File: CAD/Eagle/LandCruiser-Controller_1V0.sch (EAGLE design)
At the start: 21 parts, among them U101 MEGA8-P, X301 I2C

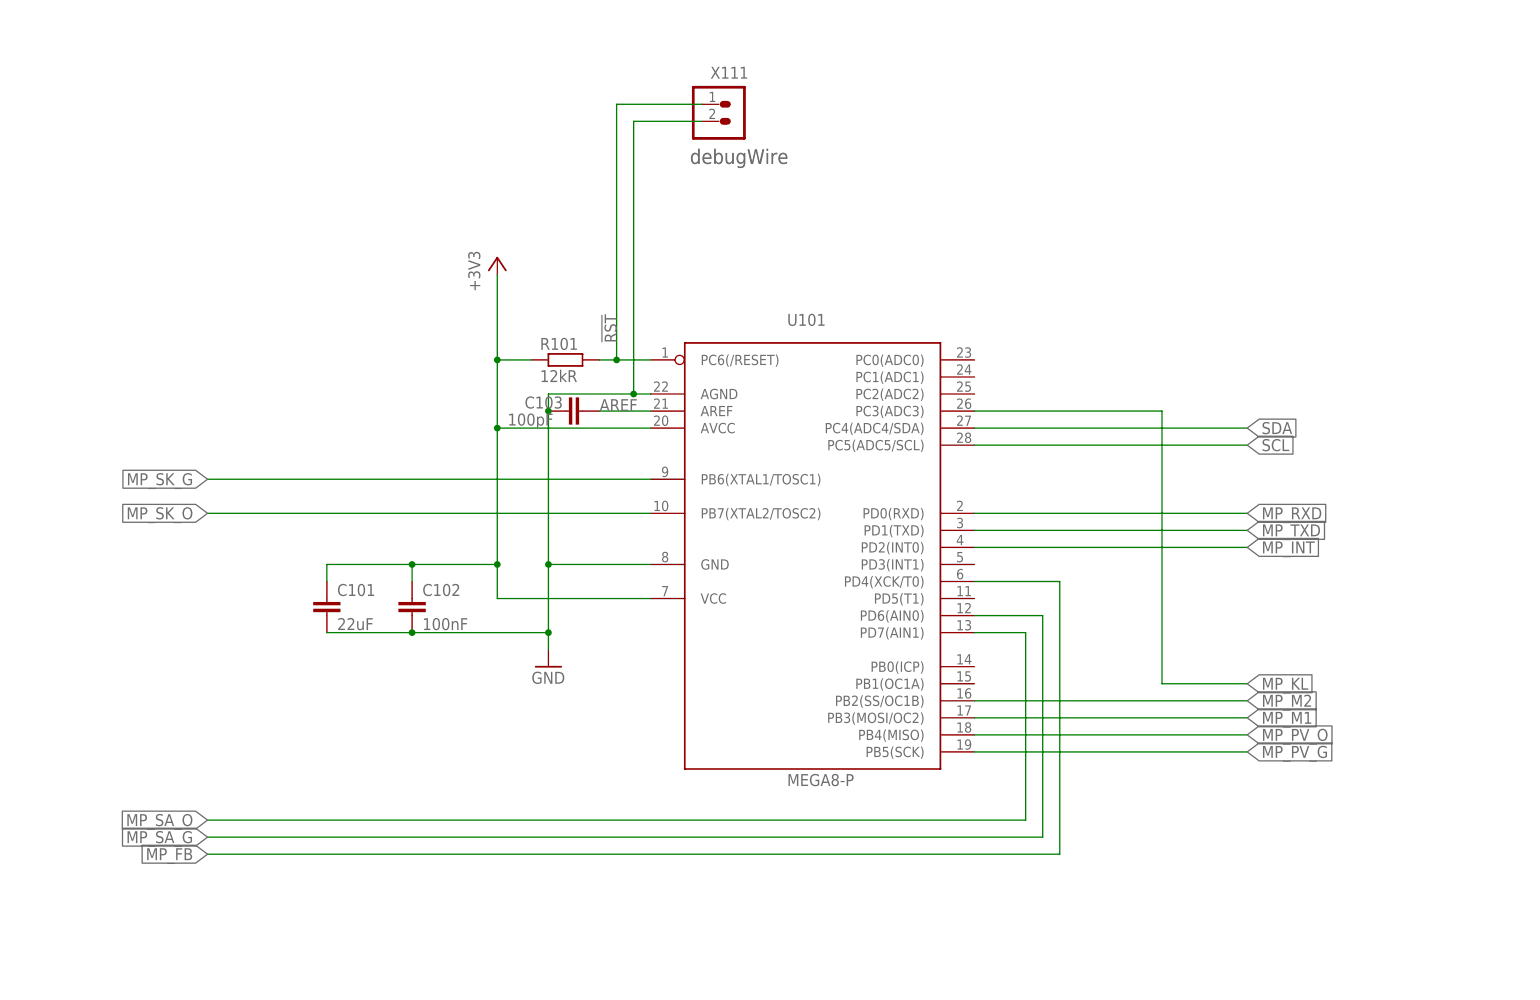
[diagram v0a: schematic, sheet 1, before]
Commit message: HW - pull-down resistors added to the ATmega output lines
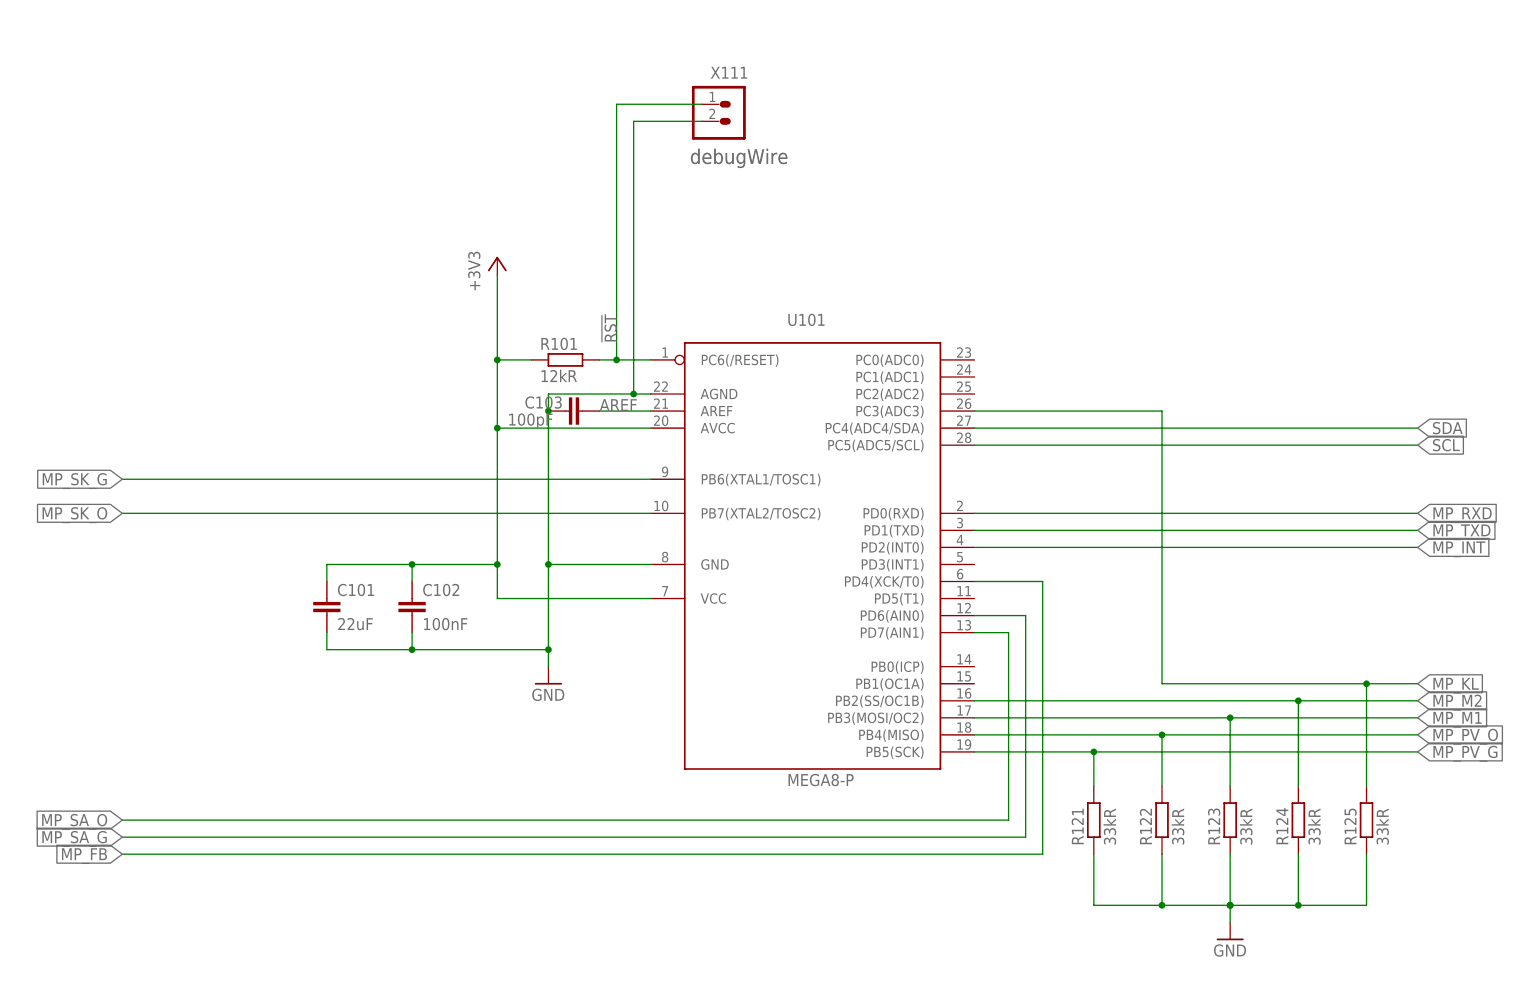
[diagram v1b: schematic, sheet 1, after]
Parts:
- added R121, R122, R123, R124, R125: 33kR, rcl:R-EU_0309/12
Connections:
- net GND: now also R121.1, R122.1, R123.1, R124.1, R125.1
- net MP_KL: now also R125.2
- net MP_M1: now also R123.2
- net MP_M2: now also R124.2
- net MP_PV_G: now also R121.2
- net MP_PV_O: now also R122.2

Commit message: HW - pull-up resistors added to the ATmega input lines
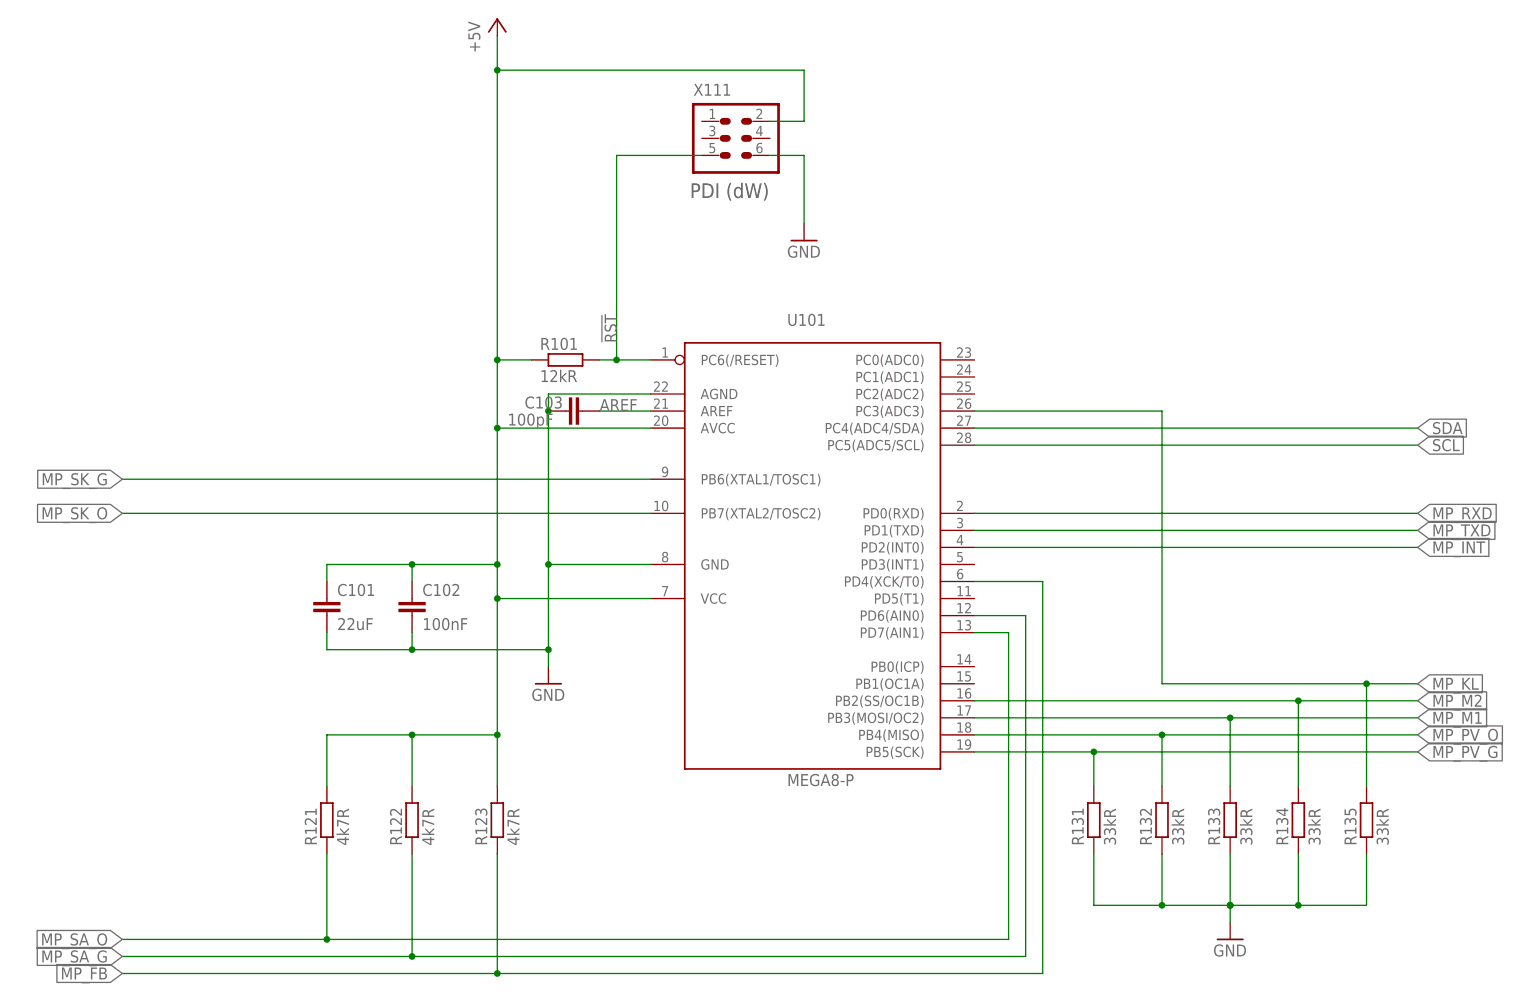
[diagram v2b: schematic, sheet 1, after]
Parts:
- removed C302: 100nF, rcl:C-EU050-035X075
- added R131, R132, R133: 33kR, rcl:R-EU_0309/12
- R121, R122, R123: value 33kR -> 4k7R
- R391, R392: value 1kR -> 2k2R
- X111: device df4iah_connector:HEADER-1X2 -> df4iah_connector:HEADER-2X3
- renumbered R124 to R134, R125 to R135
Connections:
- removed net +3V3: C101.1, C102.1, C302.1, R101.1, R391.2, R392.2, U101.AVCC, U101.VCC@1, X301.5
- net !RST: now also X111.5; no longer X111.1
- net +5V: now also C101.1, C102.1, R101.1, R121.2, R122.2, R123.2, R391.2, R392.2, U101.AVCC, U101.VCC@1, X111.2
- net GND: now also R131.1, R132.1, R133.1, X111.6; no longer C302.2, R121.1, R122.1, R123.1, X111.2
- net MP_FB: now also R123.1
- net MP_M1: now also R133.2; no longer R123.2
- net MP_PV_G: now also R131.2; no longer R121.2
- net MP_PV_O: now also R132.2; no longer R122.2
- net MP_SA_G: now also R122.1
- net MP_SA_O: now also R121.1
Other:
- note added: "PDI (dW)"
- note removed: "debugWire"
- moved on the sheet: R121, R122, R123, R391, R392

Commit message: HW - Linear voltage regulator 7805 added
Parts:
- removed C103: 100pF, rcl:C-EU050-035X075
- removed FM501, FM502, FM503, FM504: FIDUCIAL_MARK_1MM, df4iah_fiducial:FIDUCIAL_MARK_1MM
- added C501, C511: 22uF, rcl:CPOL-EUE2.5-7
- added U501: (no value), df4iah_powersupply:7805T
- C101: value 22uF -> 100nF; device rcl:C-EU150-084X183 -> rcl:C-EU050-035X075
- C102: value 100nF -> 100pF
- renumbered H501 to H603, H502 to H601, H503 to H604, H504 to H602, H511 to H611, H512 to H612
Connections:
- new net +12V: C501.+, U501.VI
- net +5V: now also C511.+, U501.VO; no longer C102.1
- net AREF: now also C102.2; no longer C103.2
- net GND: now also C102.1, C501.-, C511.-; no longer C102.2, C103.1
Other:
- note added: "X111-1 = N.C. X111-2 = VTG X111-3 = N.C. X111-4 = N.C. X111-5 = debugWIRE X111-6 = GND"

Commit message: HW - Wire-to-Board connectors added
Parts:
- added F501: 500 mA (S), fuse:SH22,5
- added R211, R212, R213, R214, R215: 12kR, rcl:R-EU_0309/12
- added X201, X321: WEIDMUELLER 1234600000, df4iah_connector:WIRE-TO-BOARD_5MM08_1X08
- renumbered C511 to C521, U501 to U511
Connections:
- new net +UB: F501.1, X201.8
- new net N$1: R211.1, X201.1
- new net N$10: X321.5
- new net N$2: R212.1, X201.2
- new net N$3: R213.1, X201.3
- new net N$4: R214.1, X201.4
- new net N$5: R215.1, X201.5
- new net N$6: X321.1
- new net N$7: X321.2
- new net N$8: X321.3
- new net N$9: X321.4
- net +12V: now also F501.2
- net GND: now also X201.7, X321.8
- net MP_KL: now also R211.2
- net MP_SA_G: now also R214.2
- net MP_SA_O: now also R215.2
- net MP_SK_G: now also R212.2
- net MP_SK_O: now also R213.2
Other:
- note added: "Weidmüller 1234600000"

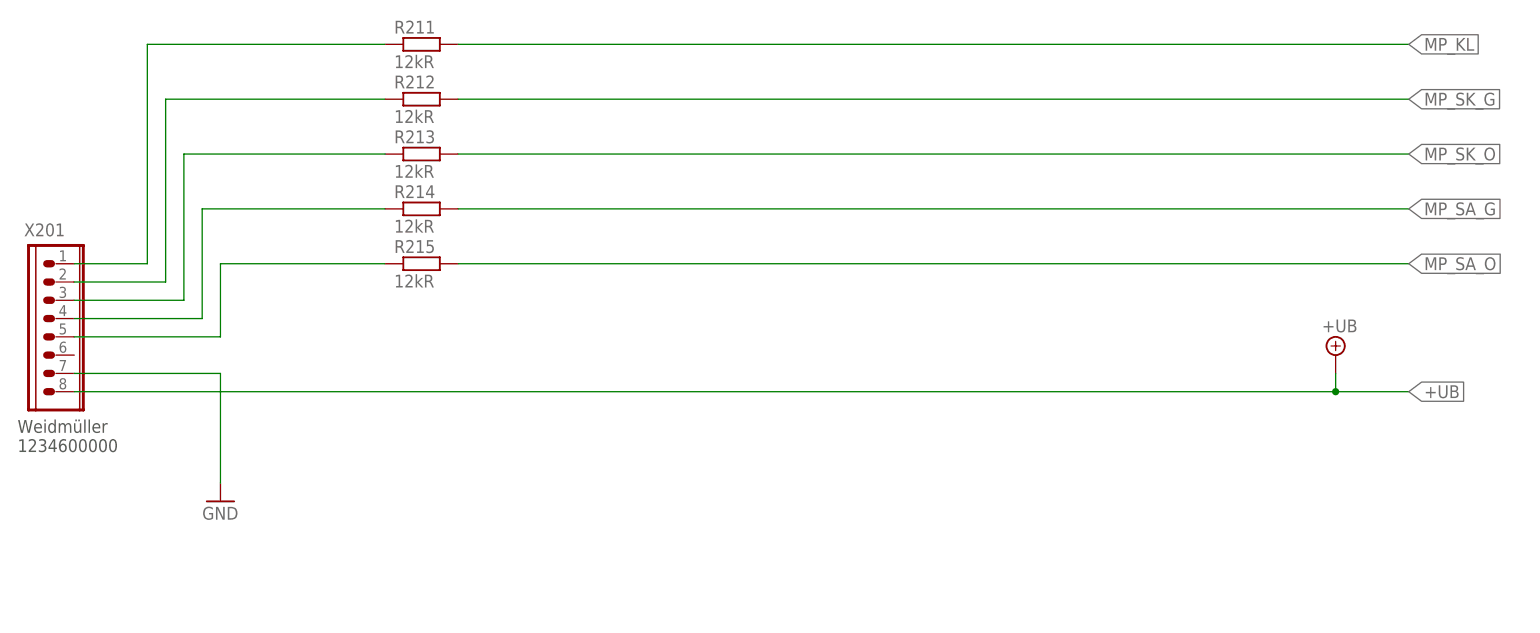
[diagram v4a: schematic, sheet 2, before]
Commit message: HW_V1.0 - ESD - circuits added
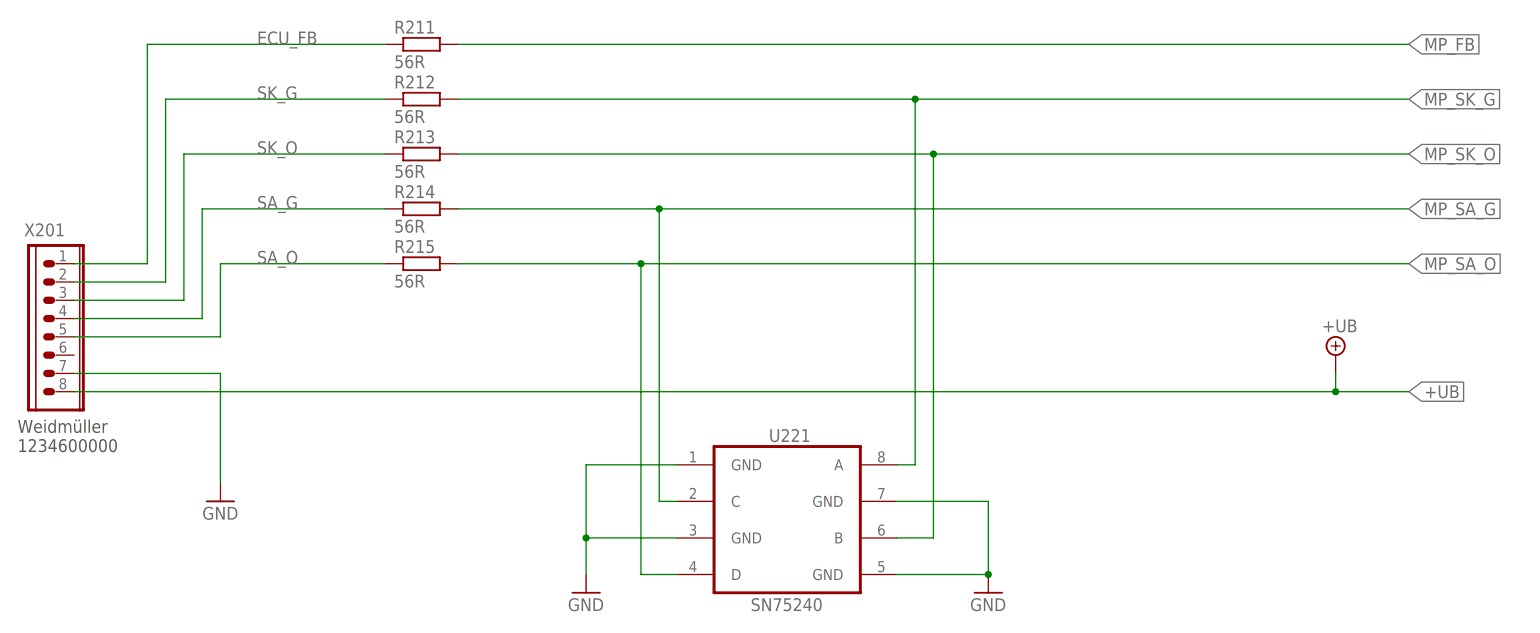
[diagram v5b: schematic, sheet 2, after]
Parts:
- added D501: 1N5817-B, df4iah_diode:1N5817-B
- added U221: SN75240, df4iah_esd:SN75240
- R211, R212, R213, R214, R215: value 12kR -> 56R
- U511: value (none) -> LM7805
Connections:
- net N$1 renamed ECU_FB
- net N$10 renamed M2
- net N$2 renamed SK_G
- net N$3 renamed SK_O
- net N$4 renamed SA_G
- net N$5 renamed SA_O
- net N$6 renamed KL
- net N$7 renamed PV_G
- net N$8 renamed PV_O
- net N$9 renamed M1
- net +12V: now also D501.C
- net GND: now also D501.A, U221.GND@1, U221.GND@3, U221.GND@5, U221.GND@7, U511.GND
- net MP_FB: now also R211.2
- net MP_KL: no longer R211.2
- net MP_SA_G: now also U221.C
- net MP_SA_O: now also U221.D
- net MP_SK_G: now also U221.A
- net MP_SK_O: now also U221.B

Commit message: HW_V1.0 - Driver - circuit added
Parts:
- added U301: MIC2981/2982, df4iah_dataconvertion:MIC2981/2982
- renumbered C301 to C401, R391 to R491, R392 to R492, X301 to X401
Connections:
- new net DRV_KL: U301.OUT1
- new net DRV_M1: U301.OUT4
- new net DRV_M2: U301.OUT5
- new net DRV_PV_G: U301.OUT2
- new net DRV_PV_O: U301.OUT3
- net +5V: now also U301.VS
- net GND: now also U301.GND, U301.IN6, U301.IN7, U301.IN8
- net MP_KL: now also U301.IN1
- net MP_M1: now also U301.IN4
- net MP_M2: now also U301.IN5
- net MP_PV_G: now also U301.IN2
- net MP_PV_O: now also U301.IN3
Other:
- note added: "X401-1 = GND X401-2 = SCL X401-3 = VCC 5.0V X401-4 = SDA X401-5 = VCC 3.3V X401-6 = GND"
- note removed: "X301-1 = GND X301-2 = SCL X301-3 = VCC 5.0V X301-4 = SDA X301-5 = VCC 3.3V X301-6 = GND"

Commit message: HW_V1.0 - Relay - pre-works done
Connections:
- net +12V: now also U301.VS
- net +5V: no longer U301.VS
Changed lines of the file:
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@@
 <part name="GND1" library="df4iah_supply" deviceset="GND" device=""/>
 <part name="U301" library="df4iah_dataconvertion" deviceset="MIC2981/2982" device=""/>
-<part name="+5V0_1" library="df4iah_supply" deviceset="+5V" device=""/>
 <part name="GND302" library="df4iah_supply" deviceset="GND" device=""/>
 <part name="GND301" library="df4iah_supply" deviceset="GND" device=""/>
+<part name="P+12V_1" library="df4iah_supply" deviceset="+12V" device=""/>
 </parts>
 <sheets>
@@
 <instance part="GND321" gate="1" x="220.98" y="73.66"/>
 <instance part="U301" gate="G$1" x="71.12" y="96.52"/>
-<instance part="+5V0_1" gate="G$1" x="48.26" y="121.92"/>
 <instance part="GND302" gate="1" x="91.44" y="66.04"/>
 <instance part="GND301" gate="1" x="40.64" y="66.04"/>
+<instance part="P+12V_1" gate="1" x="48.26" y="121.92"/>
 </instances>
 <busses>
@@
 </segment>
 </net>
-<net name="+5V" class="0">
+<net name="DRV_KL" class="0">
+<segment>
+<pinref part="U301" gate="G$1" pin="OUT1"/>
+<wire x1="86.36" y1="109.22" x2="106.68" y2="109.22" width="0.1524" layer="91"/>
+<label x="91.44" y="109.22" size="1.778" layer="95"/>
+</segment>
+</net>
+<net name="DRV_PV_G" class="0">
+<segment>
+<pinref part="U301" gate="G$1" pin="OUT2"/>
+<wire x1="86.36" y1="104.14" x2="106.68" y2="104.14" width="0.1524" layer="91"/>
+<label x="91.44" y="104.14" size="1.778" layer="95"/>
+</segment>
+</net>
+<net name="DRV_PV_O" class="0">
+<segment>
+<pinref part="U301" gate="G$1" pin="OUT3"/>
+<wire x1="86.36" y1="99.06" x2="106.68" y2="99.06" width="0.1524" layer="91"/>
+<label x="91.44" y="99.06" size="1.778" layer="95"/>
+</segment>
+</net>
+<net name="DRV_M1" class="0">
+<segment>
+<pinref part="U301" gate="G$1" pin="OUT4"/>
+<wire x1="86.36" y1="93.98" x2="106.68" y2="93.98" width="0.1524" layer="91"/>
+<label x="91.44" y="93.98" size="1.778" layer="95"/>
+</segment>
+</net>
+<net name="DRV_M2" class="0">
+<segment>
+<pinref part="U301" gate="G$1" pin="OUT5"/>
+<wire x1="86.36" y1="88.9" x2="106.68" y2="88.9" width="0.1524" layer="91"/>
+<label x="91.44" y="88.9" size="1.778" layer="95"/>
+</segment>
+</net>
+<net name="+12V" class="0">
 <segment>
 <pinref part="U301" gate="G$1" pin="VS"/>
 <wire x1="55.88" y1="68.58" x2="48.26" y2="68.58" width="0.1524" layer="91"/>
 <wire x1="48.26" y1="68.58" x2="48.26" y2="119.38" width="0.1524" layer="91"/>
-<pinref part="+5V0_1" gate="G$1" pin="+5V"/>
-</segment>
-</net>
-<net name="DRV_KL" class="0">
-<segment>
-<pinref part="U301" gate="G$1" pin="OUT1"/>
-<wire x1="86.36" y1="109.22" x2="106.68" y2="109.22" width="0.1524" layer="91"/>
-<label x="91.44" y="109.22" size="1.778" layer="95"/>
-</segment>
-</net>
-<net name="DRV_PV_G" class="0">
-<segment>
-<pinref part="U301" gate="G$1" pin="OUT2"/>
-<wire x1="86.36" y1="104.14" x2="106.68" y2="104.14" width="0.1524" layer="91"/>
-<label x="91.44" y="104.14" size="1.778" layer="95"/>
-</segment>
-</net>
-<net name="DRV_PV_O" class="0">
-<segment>
-<pinref part="U301" gate="G$1" pin="OUT3"/>
-<wire x1="86.36" y1="99.06" x2="106.68" y2="99.06" width="0.1524" layer="91"/>
-<label x="91.44" y="99.06" size="1.778" layer="95"/>
-</segment>
-</net>
-<net name="DRV_M1" class="0">
-<segment>
-<pinref part="U301" gate="G$1" pin="OUT4"/>
-<wire x1="86.36" y1="93.98" x2="106.68" y2="93.98" width="0.1524" layer="91"/>
-<label x="91.44" y="93.98" size="1.778" layer="95"/>
-</segment>
-</net>
-<net name="DRV_M2" class="0">
-<segment>
-<pinref part="U301" gate="G$1" pin="OUT5"/>
-<wire x1="86.36" y1="88.9" x2="106.68" y2="88.9" width="0.1524" layer="91"/>
-<label x="91.44" y="88.9" size="1.778" layer="95"/>
-</segment>
-</net>
+<pinref part="P+12V_1" gate="1" pin="+12V"/>
+</segment>
+</net>

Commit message: HW - V24 level shifter - new page with frame added
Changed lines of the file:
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@@
 <part name="GND301" library="df4iah_supply" deviceset="GND" device=""/>
 <part name="P+12V_1" library="df4iah_supply" deviceset="+12V" device=""/>
+<part name="FRAME7" library="df4iah_frame" deviceset="A4L-LOC" device="" value="I2C connector"/>
 </parts>
 <sheets>
@@
 </nets>
 </sheet>
+<sheet>
+<description>V24 level shifter</description>
+<plain>
+</plain>
+<instances>
+<instance part="FRAME7" gate="G$1" x="0" y="0"/>
+</instances>
+<busses>
+</busses>
+<nets>
+</nets>
+</sheet>
